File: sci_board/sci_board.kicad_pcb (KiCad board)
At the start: 4 copper layers, 80 x 80 mm, 193 parts, among them J1 Conn_01x03_Pin, J10 Conn_01x04, J2 10155435-00011LF, J3 10051922-2410EHLF, J4 10051922-2410EHLF, J5 10051922-2410EHLF, J6 PC104 Conn_02x20_Odd_Even, J7 Conn_01x04_Pin, J8 10051922-2410EHLF, J9 Conn_01x06, SW1 EVP-AA602W, SW2 EVP-AA602W, U1 STM32L496VGTx, U10 MIC2009YM6-TR, U11 MIC2009YM6-TR, U12 MIC2009YM6-TR, U13 74LVC3G04, U14 TMUX131RMGR, U15 TMUX131RMGR, U16 74LVC1G139, U17 TMUX131RMGR, U18 TMUX131RMGR, U19 TMUX131RMGR, U2 TCAN3414, U20 TMUX131RMGR, U21 TMUX131RMGR, U22 TMUX131RMGR, U23 TMUX131RMGR, U24 74LVC2G07, U25 MR25H10, U26 MT29F4G01ABAFDWB-IT:F TR, U27 TPS631000DRLR, U28 TPS631000DRLR, U29 MT29F4G01ABAFDWB-IT:F TR, U3 TCAN3414, U4 MIC2009YM6-TR, U5 MIC2009YM6-TR, U6 MIC2009YM6-TR, U7 MIC2009YM6-TR, U8 MIC2009YM6-TR, U9 MIC2009YM6-TR, X1 24MHz, X2 10MHz, X3 32.768KHZ

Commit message: clenup BOM for SCI and AUX
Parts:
- R1: value 100K -> 330K
- R12, R13: footprint Resistor_SMD:R_0603_1608Metric_Pad0.98x0.95mm_HandSolder -> Resistor_SMD:R_0402_1005Metric_Pad0.72x0.64mm_HandSolder
- R20, R24, R28: value 10K -> 100K
- moved R12 0.28 mm to (94.7, 130.9)
- moved R13 0.26 mm to (99.6, 130.9)
- moved R47 0.22 mm to (89.2, 115.9), turned to -90 degrees
- moved R48 0.18 mm to (90.5, 115.9), turned to -90 degrees
- moved R49 0.15 mm to (91.7, 115.9), turned to -90 degrees
- moved R50 0.12 mm to (93.0, 115.9), turned to -90 degrees
- moved R51 0.12 mm to (94.2, 115.9), turned to -90 degrees
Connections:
- R47 pad 1: Net-(D3-A) -> /PMIC/LED1
- R47 pad 2: /PMIC/LED1 -> Net-(D3-A)
- R48 pad 1: Net-(D4-A) -> /PMIC/LED2
- R48 pad 2: /PMIC/LED2 -> Net-(D4-A)
- R49 pad 1: Net-(D5-A) -> /PMIC/LED3
- R49 pad 2: /PMIC/LED3 -> Net-(D5-A)
- R50 pad 1: Net-(D6-A) -> /PMIC/LED4
- R50 pad 2: /PMIC/LED4 -> Net-(D6-A)
- R51 pad 1: Net-(D7-A) -> /PMIC/LED5
- R51 pad 2: /PMIC/LED5 -> Net-(D7-A)

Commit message: cleaning up bom: remove main camera port since it has not pullups and capacitors, correcting some errors in camera switch
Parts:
- removed the J8 at (120.9, 122.6)
- removed JP7, JP8: SolderJumper_3_Open, Jumper:SolderJumper-3_P2.0mm_Open_TrianglePad1.0x1.5mm
- removed NT4: NetTie_2, Project:NetTie-2_SMD_Pad0.3mm
- added R16: 10K, Resistor_SMD:R_0402_1005Metric_Pad0.72x0.64mm_HandSolder, F.Cu at (126.4, 102.3)
- added R17: 10K, Resistor_SMD:R_0402_1005Metric_Pad0.72x0.64mm_HandSolder, F.Cu at (127.1, 100.7)
- added R20: 10K, Resistor_SMD:R_0402_1005Metric_Pad0.72x0.64mm_HandSolder, F.Cu at (125.6, 85.2)
- added R21: 10K, Resistor_SMD:R_0402_1005Metric_Pad0.72x0.64mm_HandSolder, F.Cu at (127.2, 85.8)
- added R24: 10K, Resistor_SMD:R_0402_1005Metric_Pad0.72x0.64mm_HandSolder, F.Cu at (125.8, 69.0)
- added R25: 10K, Resistor_SMD:R_0402_1005Metric_Pad0.72x0.64mm_HandSolder, F.Cu at (127.4, 69.0)
- C10, C15, C3: value 1uF -> 10uF
- R27: renamed from R21; value 1K5 -> 988R
- R28: renamed from R22; value 1K5 -> 988R
- R29: renamed from R23; value 1K5 -> 988R
- R31: renamed from R25; value 1K5 -> 988R
- R32: renamed from R26; value 1K5 -> 988R
- R33: renamed from R27; value 1K5 -> 988R
- R35: renamed from R29; value 1K5 -> 988R
- R36: renamed from R30; value 1K5 -> 988R
- R37: renamed from R31; value 1K5 -> 988R
- R4, R5: value 3K9 -> 5K1
- R6, R7: value 3K9 -> 10K
- U10, U11, U12, U4, U5, U6, U7, U8, U9: value MIC2009YM6-TR -> MIC2009A-1YM6-TR
- moved C54 8.01 mm to (120.7, 120.4), turned to 0 degrees
- moved X1 5.50 mm to (120.7, 122.2), turned to 90 degrees
- moved R18 2.36 mm to (125.6, 87.4)
- moved C33 2.35 mm to (125.6, 89.7)
- moved C27 1.51 mm to (118.7, 102.1)
- moved R22 1.50 mm to (125.8, 71.5)
- moved C38 1.48 mm to (125.8, 73.7)
- moved R15 0.35 mm to (123.4, 101.1)
- moved C46 0.31 mm to (123.3, 117.8)
- moved C35 0.28 mm to (129.3, 68.8)
- moved R14 0.14 mm to (124.9, 101.0)
- moved C28 0.14 mm to (124.9, 103.2)
- renumbered J9 to J8, J10 to J9, R16 to R18, R17 to R19, R18 to R22, R19 to R23, R20 to R26, R24 to R30, R28 to R34, R32 to R38, R33 to R39, R34 to R40, R35 to R41, R36 to R42, R37 to R43, R38 to R44, R39 to R45, R40 to R46, R41 to R47, R42 to R48, R43 to R49, R44 to R50, R45 to R51, R46 to R52, R47 to R53, R48 to R54, R49 to R55, R50 to R56, R51 to R57, R52 to R58, R53 to R59, R54 to R60, R55 to R61
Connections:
- U13 pad 2: /Cameras/Multiplexer/EN_B -> /Cameras/Multiplexer/EN_C
- U13 pad 5: /Cameras/Multiplexer/EN_C -> /Cameras/Multiplexer/EN_A
- U13 pad 7: /Cameras/Multiplexer/EN_A -> /Cameras/Multiplexer/EN_B
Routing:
- net /Cameras/1V5: track 131.1 -> 101.6 mm, vias 5 -> 4
- net /Cameras/2V8: track 147.3 -> 120.3 mm, vias 5 -> 4
- net /Cameras/DCMI_07: track 72.7 -> 61.4 mm
- net /Cameras/DCMI_01: track 47.0 -> 35.7 mm
- net /Cameras/DCMI_02: track 43.1 -> 31.9 mm
- net /Cameras/DCMI_00: track 57.2 -> 46.8 mm
- net /Cameras/DCMI_03: track 52.6 -> 42.2 mm
- net /Cameras/DCMI_HSYNC: track 92.1 -> 81.8 mm
- net /Cameras/PWRDN: track 68.6 -> 58.4 mm
- net /Cameras/I2C_SCK: track 74.9 -> 64.7 mm
- net /Cameras/STROBE: track 65.1 -> 55.0 mm
- net /Cameras/RESET: track 62.6 -> 52.6 mm
- net /Cameras/DCMI_VSYNC: track 64.3 -> 54.2 mm
- net /Cameras/I2C_SDA: track 76.4 -> 66.4 mm
- net +3V3_Cameras: track 126.2 -> 116.3 mm, vias 20 -> 19
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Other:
- board text removed: "CAM"

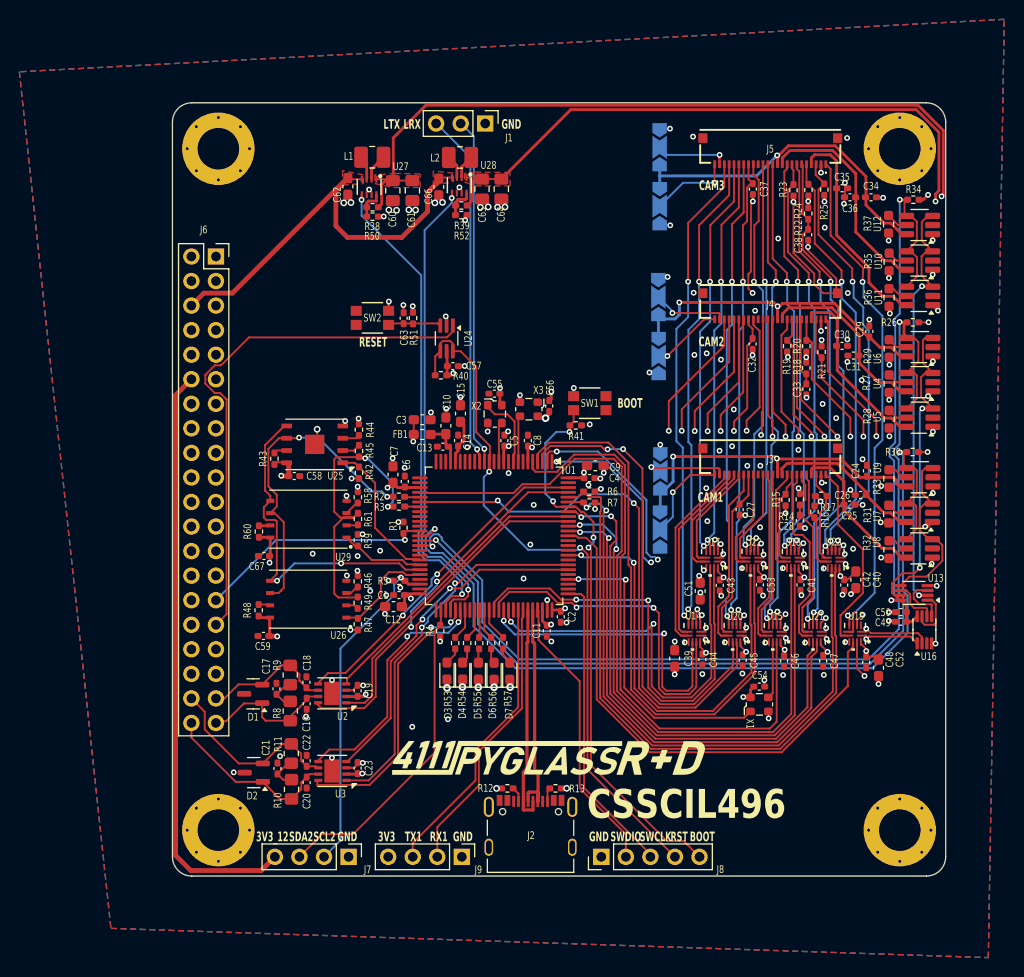
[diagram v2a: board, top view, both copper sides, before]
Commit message: QC, add second 3V regulator to AUX, INT pullups on AUX SCI AVI
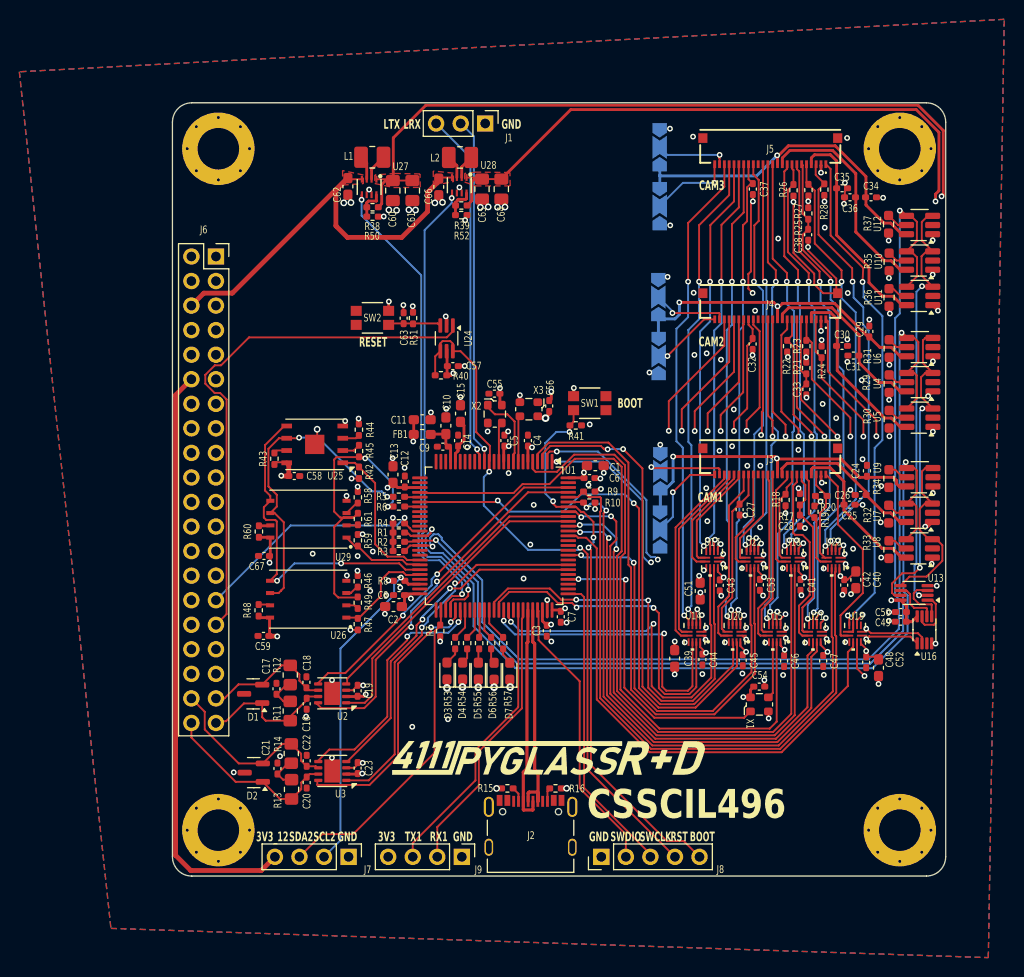
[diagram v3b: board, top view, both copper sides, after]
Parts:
- removed the R26 at (136.6, 82.7)
- removed the R30 at (136.6, 96.1)
- removed the R34 at (136.7, 70.0)
- added R1: 100K, Resistor_SMD:R_0402_1005Metric_Pad0.72x0.64mm_HandSolder, F.Cu at (83.4, 104.5)
- added R2: 100K, Resistor_SMD:R_0402_1005Metric_Pad0.72x0.64mm_HandSolder, F.Cu at (83.4, 105.4)
- added R3: 100K, Resistor_SMD:R_0402_1005Metric_Pad0.72x0.64mm_HandSolder, F.Cu at (83.4, 106.4)
- SW1: footprint Project:EVP602AA -> Common:EVP602AA
- moved R4 0.66 mm to (83.4, 103.5), turned to 0 degrees
- renumbered C9 to C1, C3 to C11, C6 to C12, C7 to C13, C12 to C2, C11 to C3, C8 to C4, C4 to C6, C2 to C7, C1 to C8, C13 to C9, R7 to R10, R8 to R11, R9 to R12, R10 to R13, R11 to R14, R12 to R15, R13 to R16, R14 to R17, R15 to R18, R16 to R19, R17 to R20, R18 to R21, R19 to R22, R20 to R23, R21 to R24, R22 to R25, R23 to R26, R24 to R27, R25 to R28, R27 to R29, R28 to R30, R29 to R31, R31 to R32, R32 to R33, R33 to R34, R1 to R4, R2 to R5, R3 to R6, R4 to R7, R5 to R8, R6 to R9
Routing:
- net +3V3_STM32_Core: track 33.8 -> 36.7 mm
- net +3V3_Cameras: track 116.3 -> 114.1 mm, vias 19 -> 16
- net /INT1: track 95.0 -> 93.3 mm
- net /INT2: track 104.4 -> 102.8 mm
- net /INT3: track 116.7 -> 115.2 mm
- net /ATTN: track 24.3 -> 25.6 mm
- net /MRAM/SPI_CS: track 14.6 -> 15.6 mm

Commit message: tweaks before merge
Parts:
- H1, H2, H3, H4: footprint Project:MountingHole_4.3mm_M4_Pad_Via_Custom -> Common:MountingHole_4.3mm_M4_Pad_Via_Custom
- J2: footprint Project:AMPHENOL_10155435-00011LF -> Common:AMPHENOL_10155435-00011LF
- J3, J4, J5: footprint Project:100519222410EHLF -> Common:100519222410EHLF
- NT1, NT2, NT3: footprint Project:NetTie-2_SMD_Pad0.3mm -> Common:NetTie-2_SMD_Pad0.3mm
- SW2: footprint Project:EVP602AA -> Common:EVP602AA
- U14, U15, U17, U18, U19, U20, U21, U22, U23: footprint Project:VQFN12_RMG_TEX -> Common:VQFN12_RMG_TEX
- moved C66 3.77 mm to (89.0, 72.2)
- moved C64 3.77 mm to (95.5, 72.4)
- moved C65 3.77 mm to (93.5, 72.4)
- moved L2 3.77 mm to (91.2, 69.1)
- moved R39 3.77 mm to (91.3, 74.1)
- moved R52 3.77 mm to (91.3, 75.1)
- moved U28 3.77 mm to (91.1, 72.0)
- moved L1 3.49 mm to (80.7, 69.1)
- moved R38 3.49 mm to (80.7, 74.3)
- moved C60 3.49 mm to (82.8, 72.6)
- moved C61 3.49 mm to (84.8, 72.6)
- moved C62 3.49 mm to (78.1, 72.1)
- moved R50 3.49 mm to (80.7, 75.3)
- moved U27 3.49 mm to (80.3, 72.2)
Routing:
- net +BATT: track 44.4 -> 36.2 mm, vias 0 -> 2
- net /Cameras/EN_2V8: track 49.5 -> 45.8 mm
- net /Cameras/EN_1V5: track 48.7 -> 45.8 mm
- net /Cameras/1V5: track 101.6 -> 98.8 mm
- net /Cameras/2V8: track 120.3 -> 117.8 mm
- net /PMIC/LPUART_TX: track 36.9 -> 37.5 mm
- net /Cameras/Multiplexer/EN_C: track 43.3 -> 42.7 mm
- net GND: vias 155 -> 156
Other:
- board text removed: "23"
- board text removed: "24"
